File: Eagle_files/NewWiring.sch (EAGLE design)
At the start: 69 parts, among them T1 PIN, T2 PIN

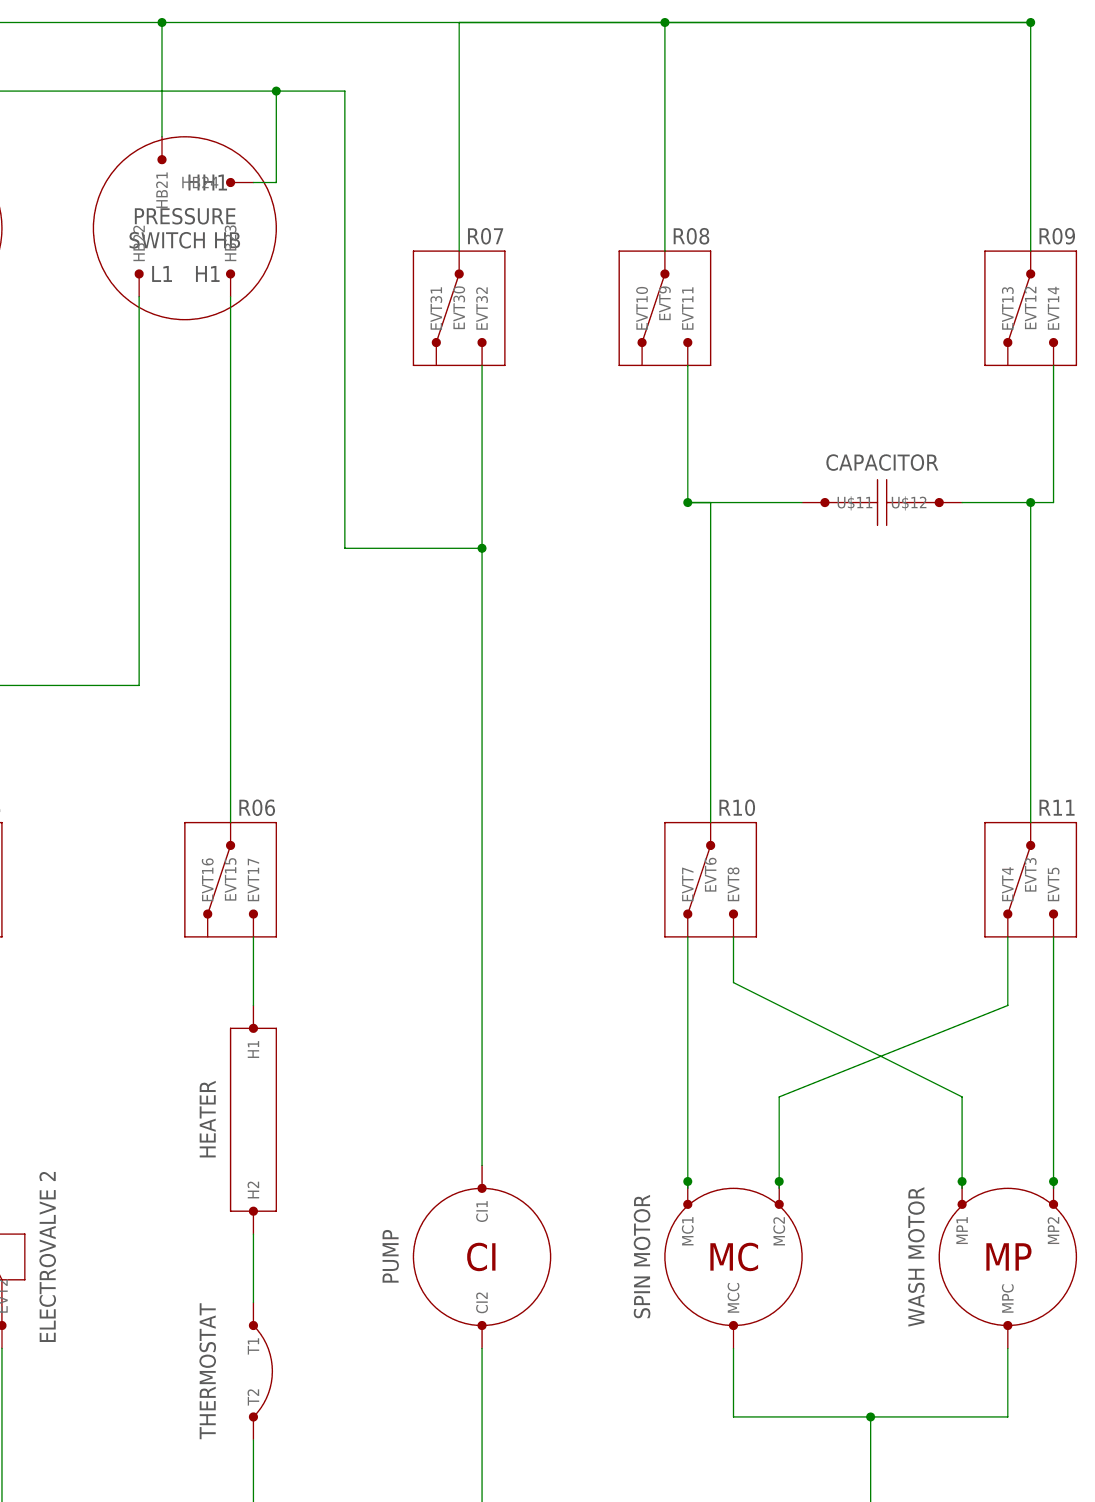
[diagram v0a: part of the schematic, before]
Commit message: Modified wiring of R08 and R09
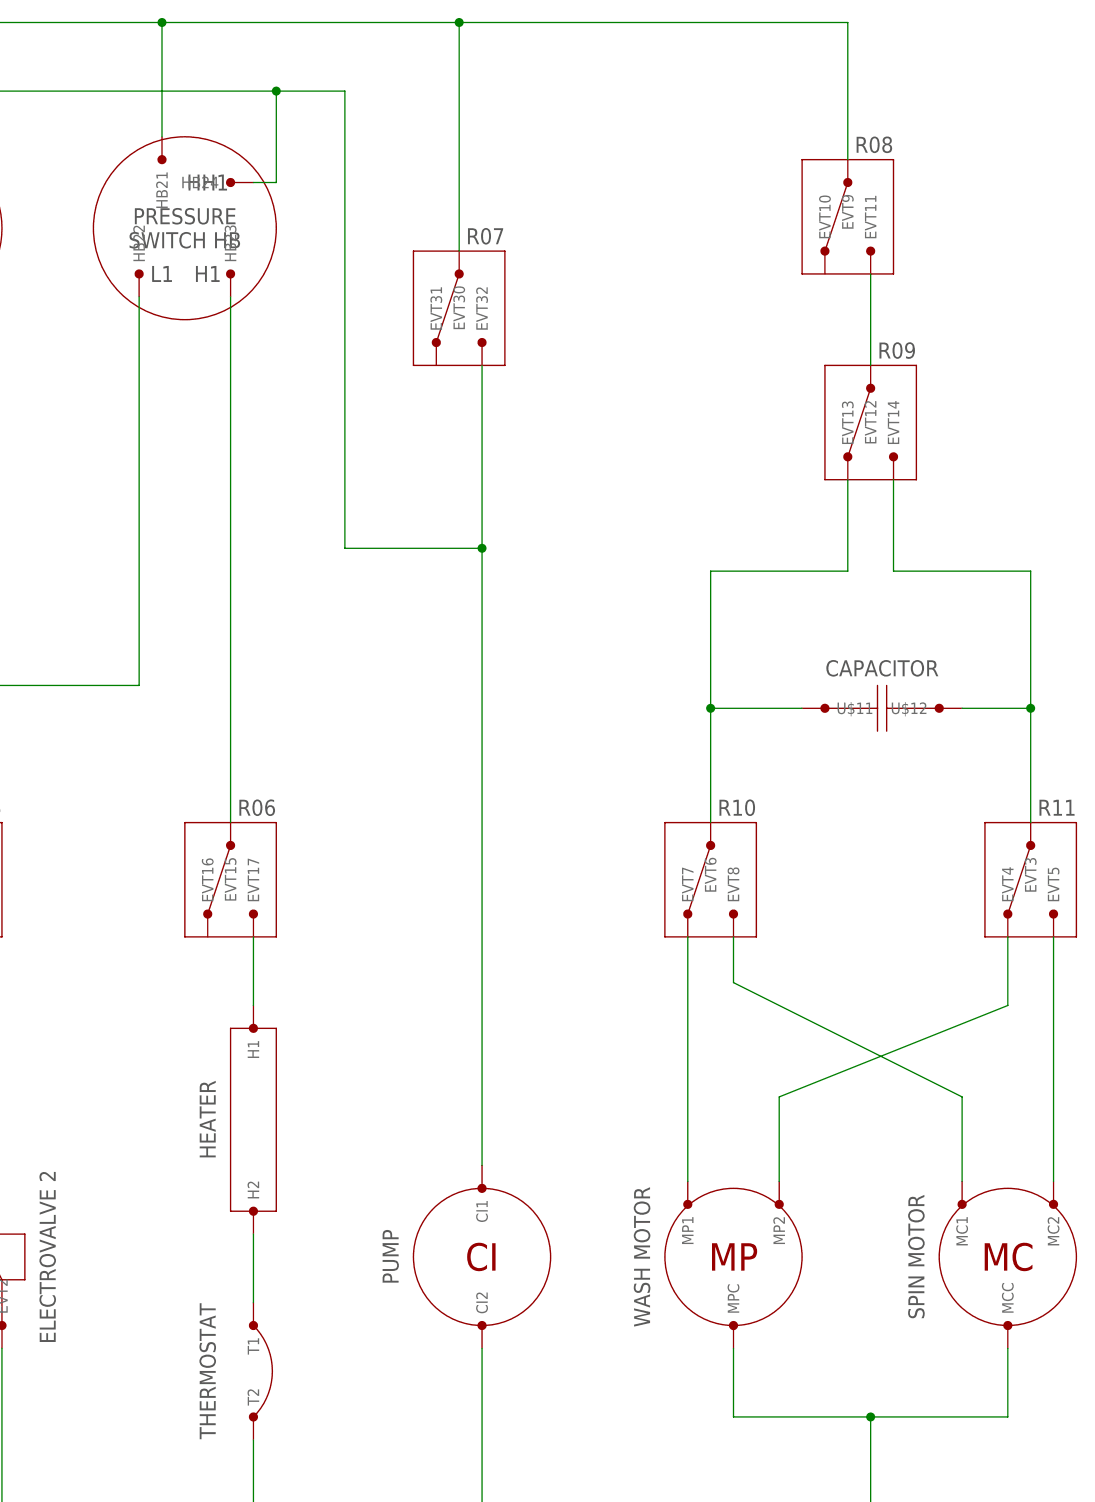
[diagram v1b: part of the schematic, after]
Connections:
- removed net N$13: EVT5.PIN1, MP2.PIN1
- new net N$7: EVT7.PIN1, MP1.PIN1
- new net N$9: EVT5.PIN1, MC2.PIN1
- net N$11: now also EVT8.PIN1; no longer EVT7.PIN1
- net N$12: now also EVT11.PIN1, EVT12.PIN1; no longer EVT8.PIN1, MP1.PIN1
- net N$14: now also MP2.PIN1; no longer MC2.PIN1
- net N$16: now also EVT13.PIN1; no longer EVT11.PIN1
- net NEUTRAL: no longer EVT12.PIN1
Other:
- moved on the sheet: EVT10, EVT11, EVT12, EVT13, EVT14, EVT9, MC1, MC2, MCC, MP1, MP2, MPC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

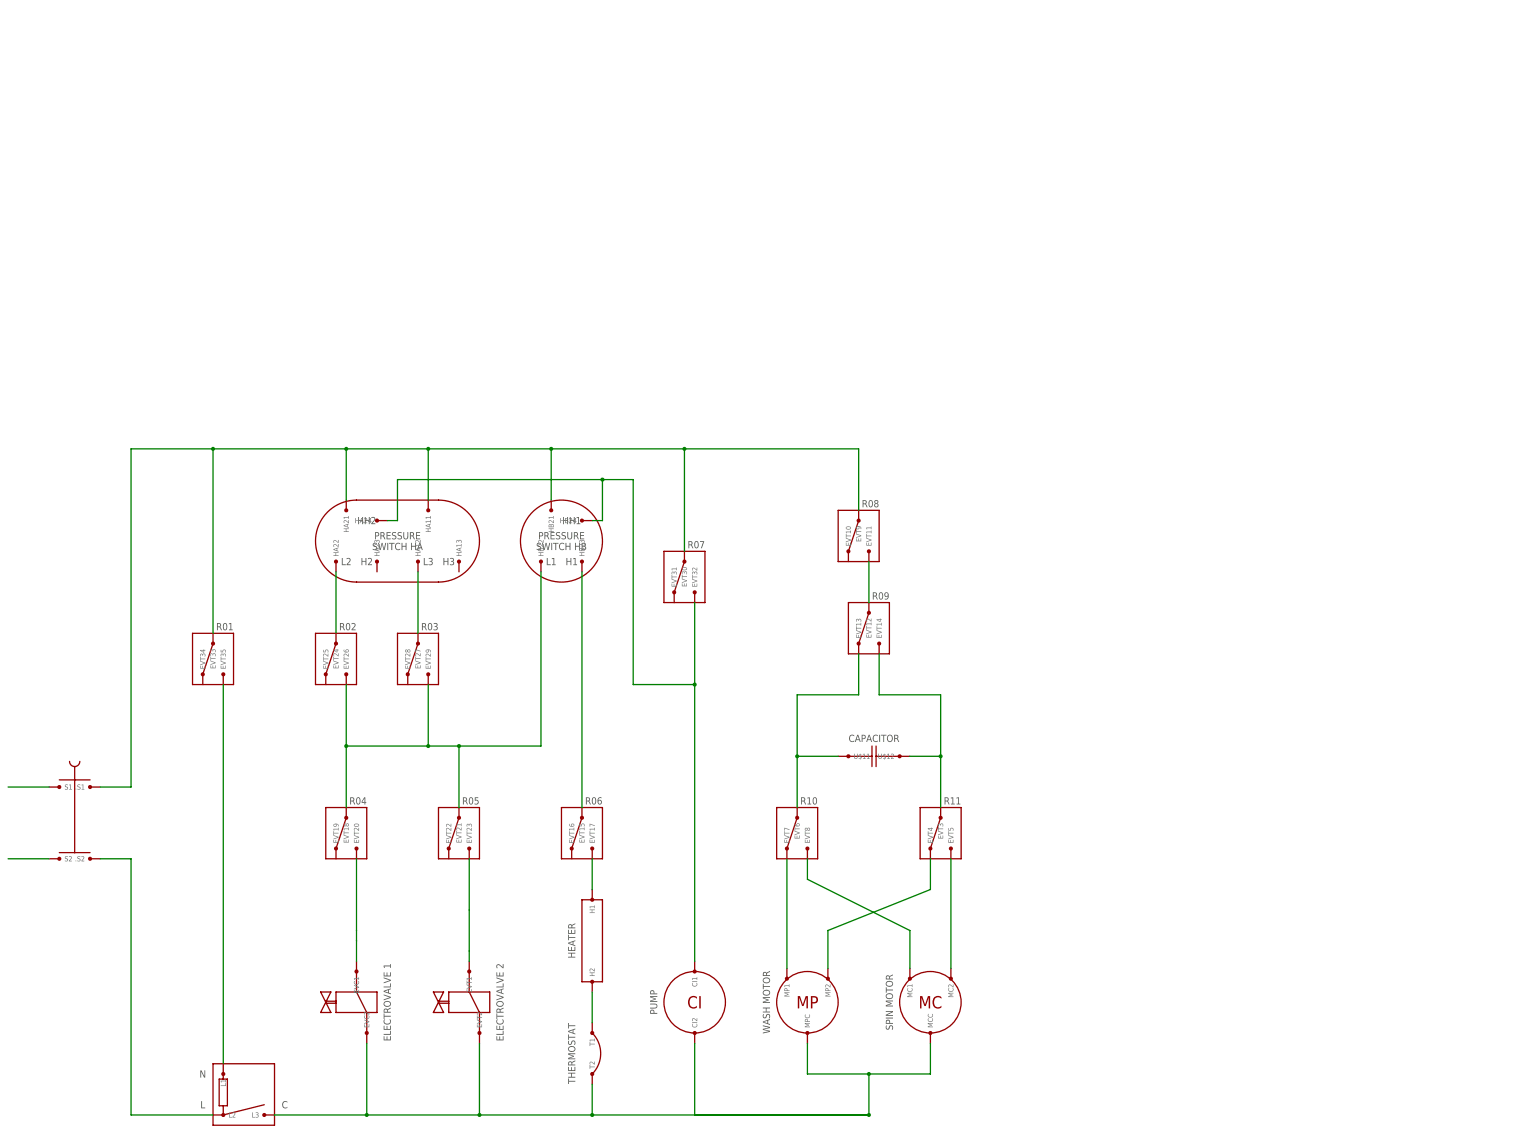
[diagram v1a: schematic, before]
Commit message: Added connectors
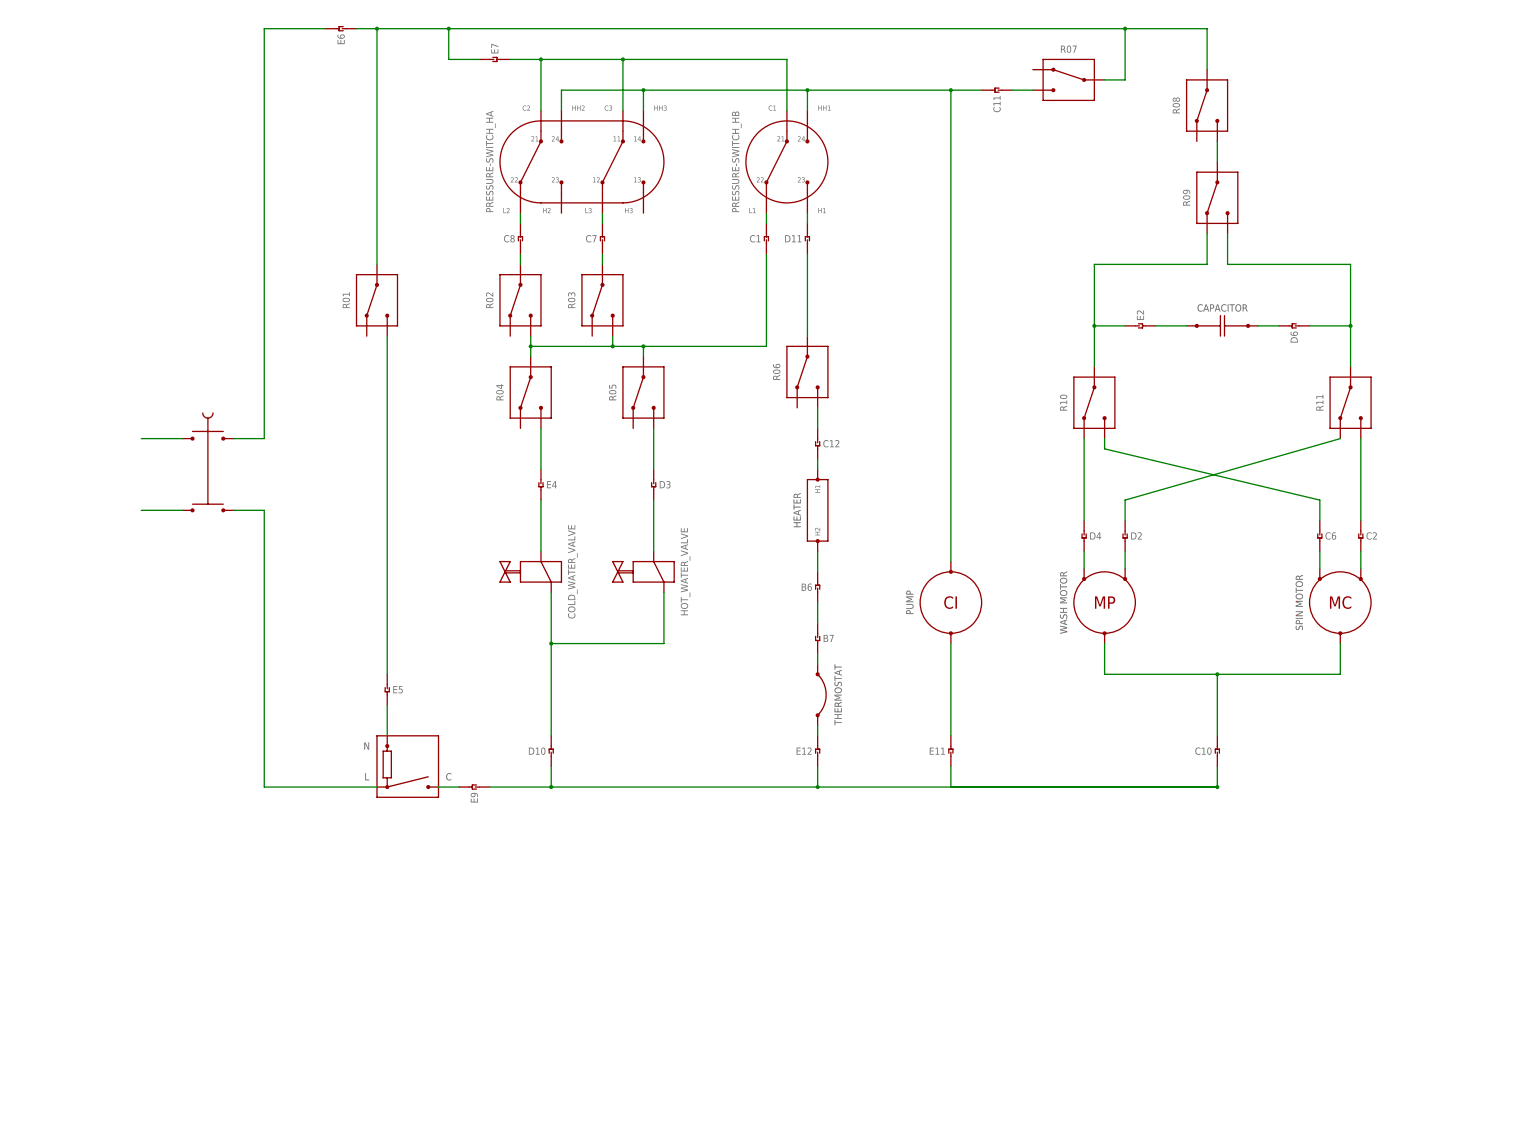
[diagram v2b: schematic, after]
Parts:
- removed EVC1, EVC2, EVT1, EVT10, EVT11, EVT12, EVT13, EVT14, EVT15, EVT16, EVT17, EVT18, EVT19, EVT2, EVT20, EVT21, EVT22, EVT23, EVT24, EVT25, EVT26, EVT27, EVT28, EVT29, EVT3, EVT30, EVT31, EVT32, EVT33, EVT34, EVT35, EVT4, EVT5, EVT6, EVT7, EVT8, EVT9, HA11, HA12, HA13, HA21, HA22, HA23, HA24, HB21, HB22, HB23, HB24: PIN, Connectors:PIN
- added B6, B7, C1, C10, C11, C12, C2, C6, C7, C8, D10, D11, D2, D3, D4, D6, E11, E12, E2, E4, E5, E6, E7, E9: CABLE, Kostas:CABLE
- added COLD_WATER_VALVE, HOT_WATER_VALVE: VALVE, Kostas:VALVE
- added PRESSURE-SWITCH_HA: PS2, Kostas:PS2
- added PRESSURE-SWITCH_HB: PS1, Kostas:PS1
- added R01, R02, R03, R04, R05, R06, R07, R08, R09, R10, R11: RELAY, Kostas:RELAY
- .S1, .S2, CI1, CI2, L1, L2, L3, MC1, MC2, MCC, MP1, MP2, MPC, S1, S2, T1, T2, U$11, U$12: device Connectors:PIN -> Kostas:PIN
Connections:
- removed net N$5: H2.PIN1, T1.PIN1
- removed net OVERFLOW: CI1.PIN1, EVT32.PIN1, HA24.PIN1, HB24.PIN1
- removed net PHASE1: EVT15.PIN1, HB23.PIN1
- new net B7: B7.PIN2, T1.PIN1
- new net C1: C1.PIN2, PRESSURE-SWITCH_HB.P$3
- new net C10: C10.PIN2, MCC.PIN1, MPC.PIN1
- new net C11-OVERFLOW: C11.PIN2, CI1.PIN1, PRESSURE-SWITCH_HA.P$2, PRESSURE-SWITCH_HA.P$6, PRESSURE-SWITCH_HB.P$2
- new net C2: C2.PIN2, MC2.PIN1
- new net C6: C6.PIN2, MC1.PIN1
- new net D10: COLD_WATER_VALVE.P$1, D10.PIN2, HOT_WATER_VALVE.P$1
- new net D11: D11.PIN2, PRESSURE-SWITCH_HB.P$4
- new net D2: D2.PIN2, MP2.PIN1
- new net D4: D4.PIN2, MP1.PIN1
- new net D6: D6.PIN2, U$12.PIN1
- new net E11: CI2.PIN1, E11.PIN2
- new net E5: E5.PIN2, L1.PIN1
- new net N$13: B6.PIN1, B7.PIN1
- new net N$20: E9.PIN2, L3.PIN1
- new net N$21: C12.PIN2, H1.PIN1
- new net N$22: E12.PIN2, T2.PIN1
- new net N$23: C12.PIN1, R06.P$3
- new net N$24: C11.PIN1, R07.P$3
- new net N$25: D3.PIN1, R05.P$3
- new net N$27: B6.PIN2, H2.PIN1
- new net N$33: E2.PIN2, U$11.PIN1
- new net N$39: E7.PIN2, PRESSURE-SWITCH_HA.P$1, PRESSURE-SWITCH_HA.P$5, PRESSURE-SWITCH_HB.P$1
- new net N$42: C8.PIN1, R02.P$1
- new net N$43: C7.PIN1, R03.P$1
- new net N$45: D11.PIN1, R06.P$1
- new net N$47: E4.PIN1, R04.P$3
- net LIVE: now also C10.PIN1, D10.PIN1, E11.PIN1, E12.PIN1, E9.PIN1; no longer CI2.PIN1, EVC2.PIN1, EVT2.PIN1, L3.PIN1, MCC.PIN1, MPC.PIN1, T2.PIN1
- net N$1: now also .S1.PIN1, E6.PIN2; no longer EVT17.PIN1, H1.PIN1
- net N$11: now also C6.PIN1, R10.P$3; no longer EVT8.PIN1, MC1.PIN1
- net N$12: now also R08.P$3, R09.P$1; no longer EVT11.PIN1, EVT12.PIN1
- net N$14: now also D2.PIN1, R11.P$2; no longer EVT4.PIN1, MP2.PIN1
- net N$15: now also D6.PIN1, R09.P$3, R11.P$1; no longer EVT14.PIN1, EVT3.PIN1, U$12.PIN1
- net N$16: now also E2.PIN1, R09.P$2, R10.P$1; no longer EVT13.PIN1, EVT6.PIN1, U$11.PIN1
- net N$17: now also C8.PIN2, PRESSURE-SWITCH_HA.P$3; no longer EVT24.PIN1, HA22.PIN1
- net N$18: now also C7.PIN2, PRESSURE-SWITCH_HA.P$7; no longer EVT27.PIN1, HA12.PIN1
- net N$2: now also COLD_WATER_VALVE.P$2, E4.PIN2; no longer EVC1.PIN1, EVT20.PIN1
- net N$4: now also D3.PIN2, HOT_WATER_VALVE.P$2; no longer EVT1.PIN1, EVT23.PIN1
- net N$6: now also E5.PIN1, R01.P$3; no longer EVT35.PIN1, L1.PIN1
- net N$7: now also D4.PIN1, R10.P$2; no longer EVT7.PIN1, MP1.PIN1
- net N$9: now also C2.PIN1, R11.P$3; no longer EVT5.PIN1, MC2.PIN1
- net NEUTRAL: now also E6.PIN1, E7.PIN1, R01.P$1, R07.P$1, R08.P$1; no longer .S1.PIN1, EVT30.PIN1, EVT33.PIN1, EVT9.PIN1, HA11.PIN1, HA21.PIN1, HB21.PIN1
- net PHASE3: now also C1.PIN1, R02.P$3, R03.P$3, R04.P$1, R05.P$1; no longer EVT18.PIN1, EVT21.PIN1, EVT26.PIN1, EVT29.PIN1, HB22.PIN1
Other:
- note removed: "ELECTROVALVE 1"
- note removed: "ELECTROVALVE 2"
- note removed: "H1"
- note removed: "H2"
- note removed: "H3"
- note removed: "HH1"
- note removed: "HH2"
- note removed: "L1"
- note removed: "L2"
- note removed: "L3"
- note removed: "PRESSURE SWITCH HA"
- note removed: "PRESSURE SWITCH HB"
- note removed: "R01"
- note removed: "R02"
- note removed: "R03"
- note removed: "R04"
- note removed: "R05"
- note removed: "R06"
- note removed: "R07"
- note removed: "R08"
- note removed: "R09"
- note removed: "R10"
- note removed: "R11"
- moved on the sheet: H1, H2
